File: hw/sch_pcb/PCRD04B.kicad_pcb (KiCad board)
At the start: 2 copper layers, 60.5 x 40.1 mm, 62 parts, among them J1 3.6V, J11 HEADER_2x01_PARALLEL, J2 HEADER_2x01_PARALLEL, J3 HEADER_2x01_PARALLEL, J4 HEADER_2x01_PARALLEL, J5 HEADER_2x01_PARALLEL, J6 HEADER_2x01_PARALLEL, J7 HEADER_2x01_PARALLEL, M1 HOLE, M2 HOLE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

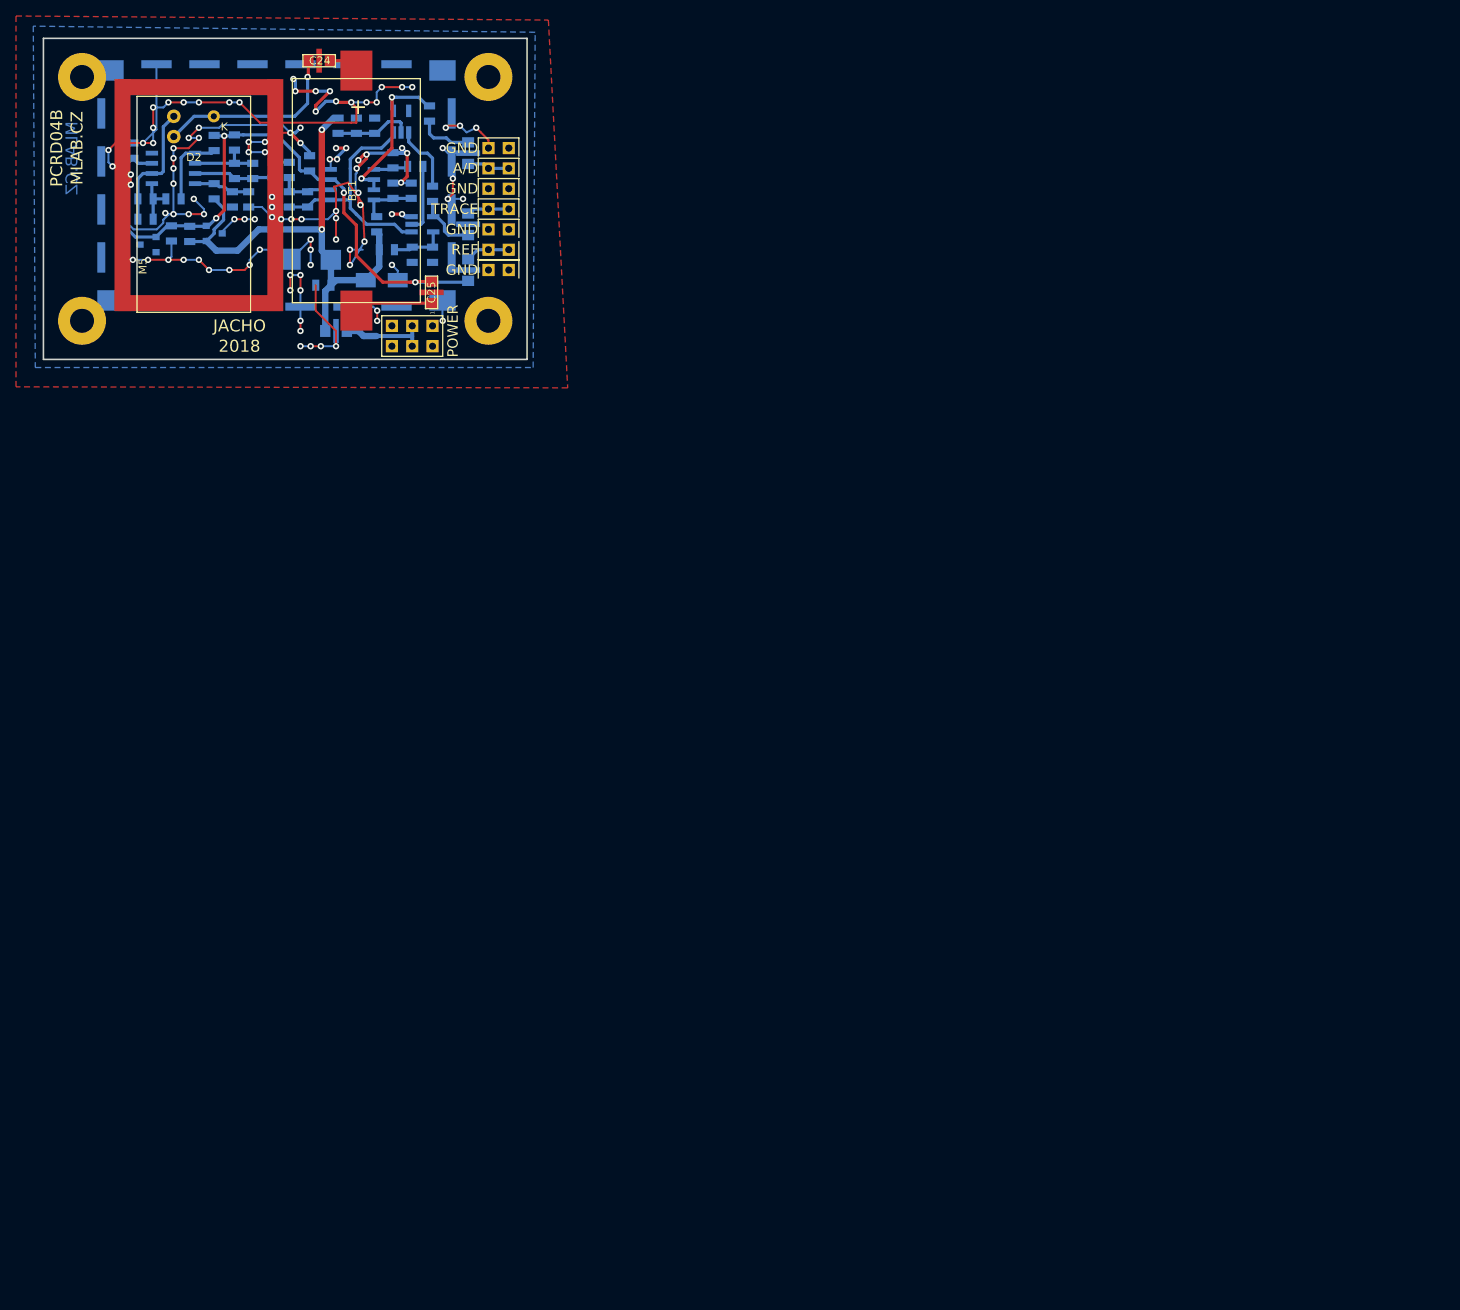
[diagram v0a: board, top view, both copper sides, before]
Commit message: clean and update templates
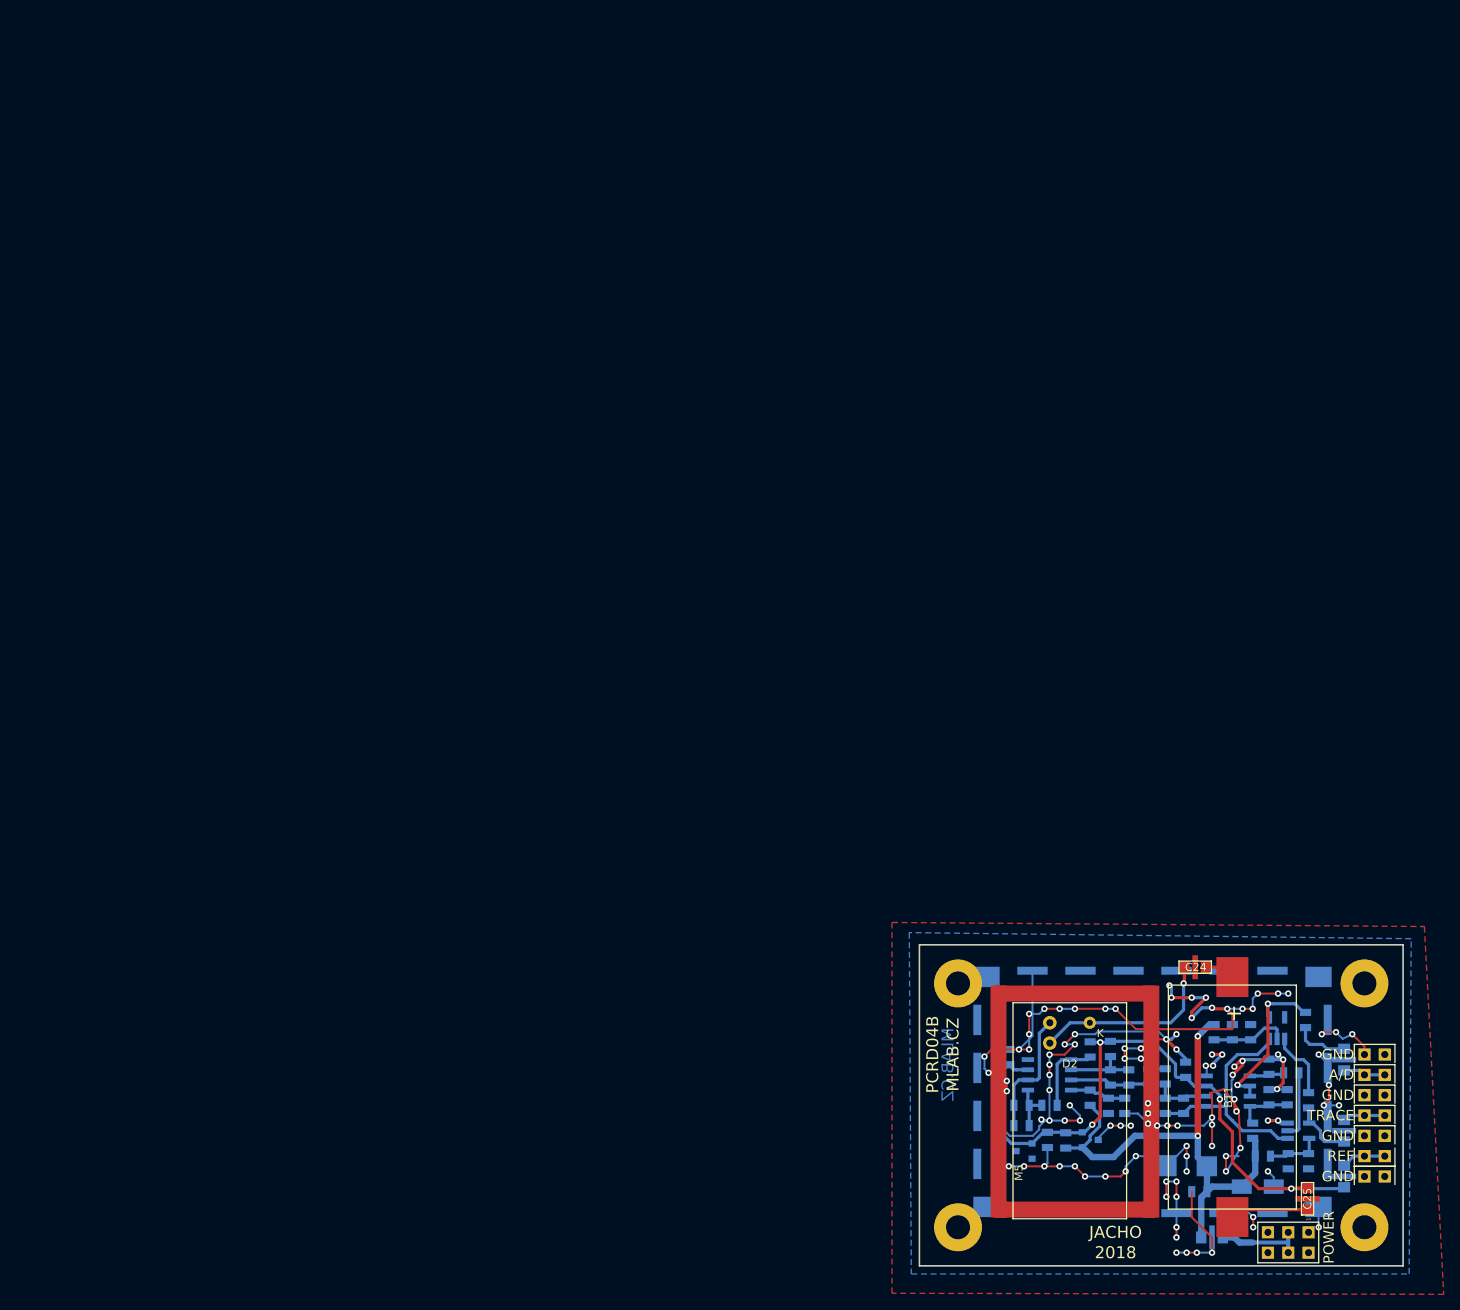
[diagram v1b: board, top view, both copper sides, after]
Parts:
- moved J1 157.6 mm to (155.9, 110.1)
- moved M3 157.6 mm to (165.4, 108.2)
- moved R3 157.6 mm to (151.4, 96.2)
- moved R8 157.6 mm to (133.6, 85.9)
- moved U2 157.6 mm to (148.4, 91.2)
- moved U3 157.6 mm to (131.1, 97.3)
- moved BT1 157.6 mm to (148.9, 92.0)
- moved C1 157.6 mm to (143.2, 100.6)
- moved C10 157.6 mm to (126.0, 93.0)
- moved C11 157.6 mm to (133.4, 93.1)
- moved C12 157.6 mm to (153.4, 92.0)
- moved C13 157.6 mm to (151.2, 83.8)
- moved C14 157.6 mm to (158.4, 100.0)
- moved C15 157.6 mm to (135.9, 89.5)
- moved C16 157.6 mm to (138.5, 89.4)
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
